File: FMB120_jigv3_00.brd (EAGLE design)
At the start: 80 x 50 mm, 9 parts, among them CN2 CP3512, SW1 switch, SW2 switch

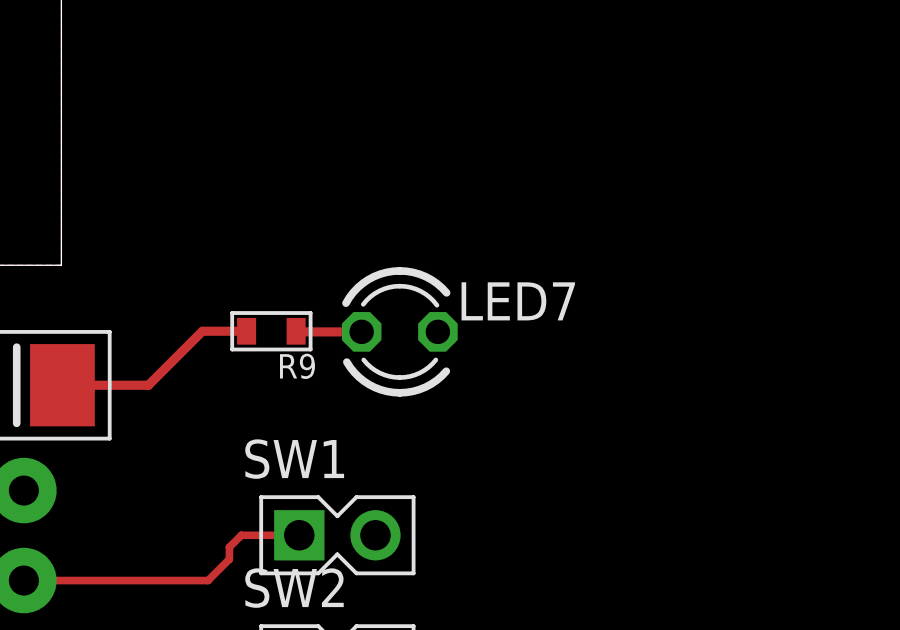
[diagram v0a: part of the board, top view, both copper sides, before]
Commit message: moved power LED up 1mm
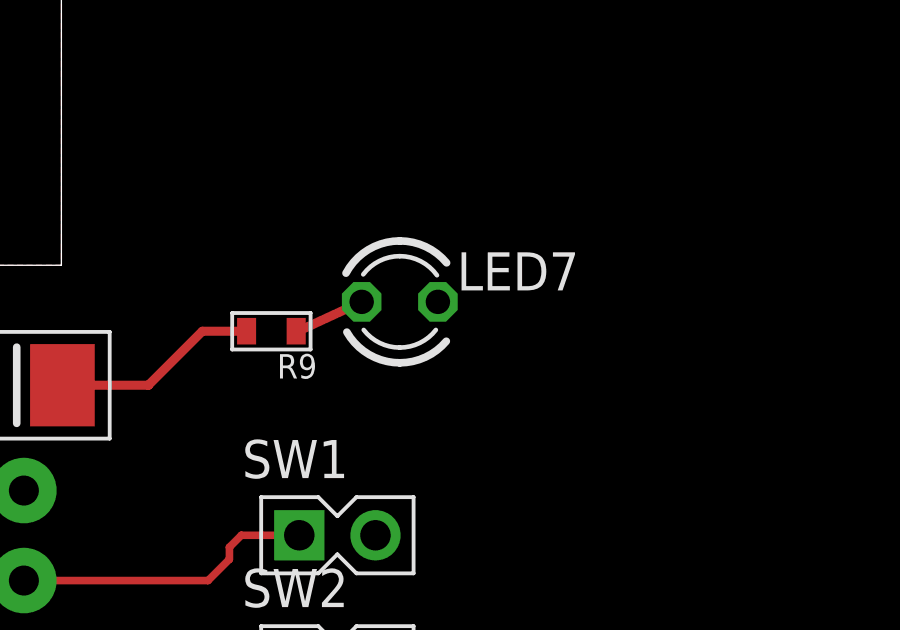
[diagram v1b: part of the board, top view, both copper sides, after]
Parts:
- moved LED7 1.00 mm to (21.3, 38.8)
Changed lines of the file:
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@@
 <setting verticaltext="up"/>
 </settings>
-<grid distance="0.1" unitdist="mm" unit="mm" style="lines" multiple="1" display="yes" altdistance="0.025" altunitdist="inch" altunit="inch"/>
+<grid distance="1" unitdist="mm" unit="mm" style="lines" multiple="1" display="yes" altdistance="0.025" altunitdist="inch" altunit="inch"/>
 <layers>
 <layer number="1" name="Top" color="4" fill="1" visible="yes" active="yes"/>
@@
 </autorouter>
 <elements>
-<element name="LED7" library="led" package="LED3MM" value="" x="21.28" y="37.78"/>
+<element name="LED7" library="led" package="LED3MM" value="" x="21.28" y="38.78"/>
 <element name="LED8" library="led" package="LED3MM" value="" x="19.72" y="10.88"/>
 <element name="LED9" library="led" package="LED3MM" value="" x="19.54" y="20.82" rot="R180"/>
@@
 <contactref element="R9" pad="1"/>
 <wire x1="17.8255" y1="37.8" x2="17.8455" y2="37.78" width="0.3048" layer="1"/>
-<wire x1="17.8455" y1="37.78" x2="20.01" y2="37.78" width="0.3048" layer="1"/>
+<wire x1="17.8455" y1="37.78" x2="20.01" y2="38.78" width="0.3048" layer="1"/>
 </signal>
 </signals>
